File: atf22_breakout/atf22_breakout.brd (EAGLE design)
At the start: 18.8 x 36.8 mm, 4 parts

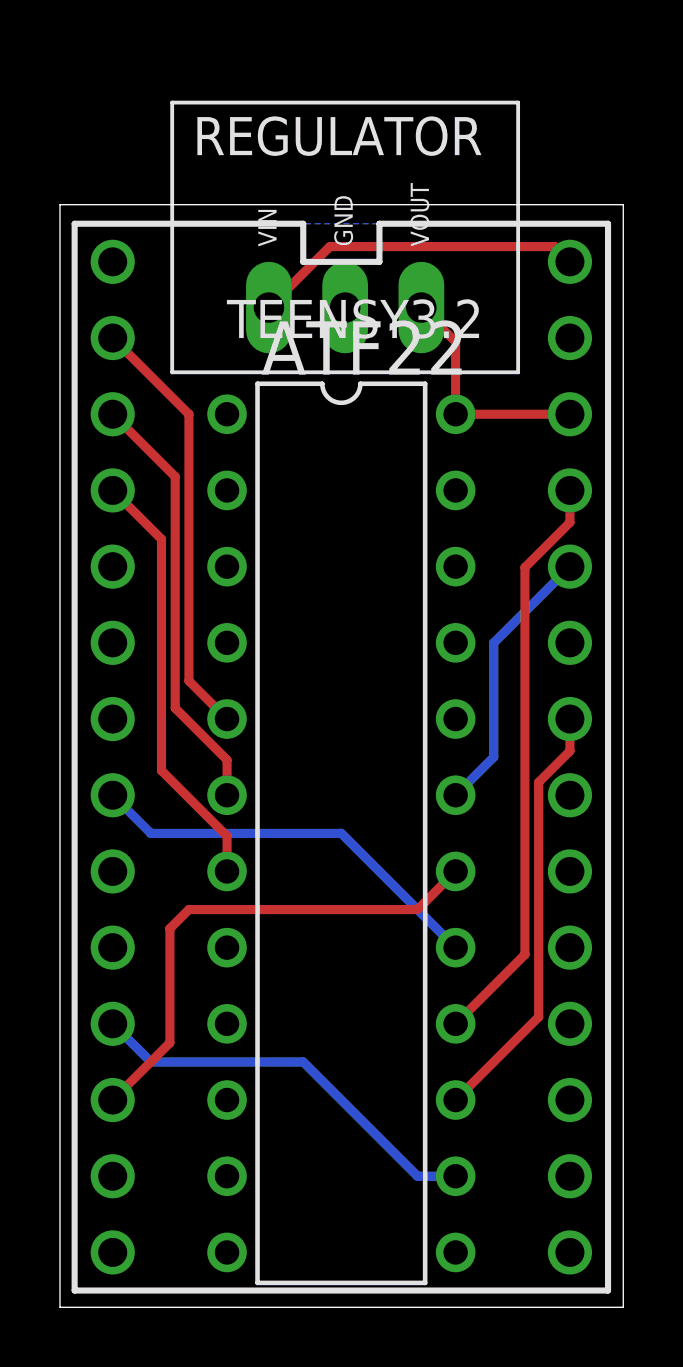
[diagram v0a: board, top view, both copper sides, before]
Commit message: Fixed ATF22 Breakout
Moved voltage regulator so it fits on the board.
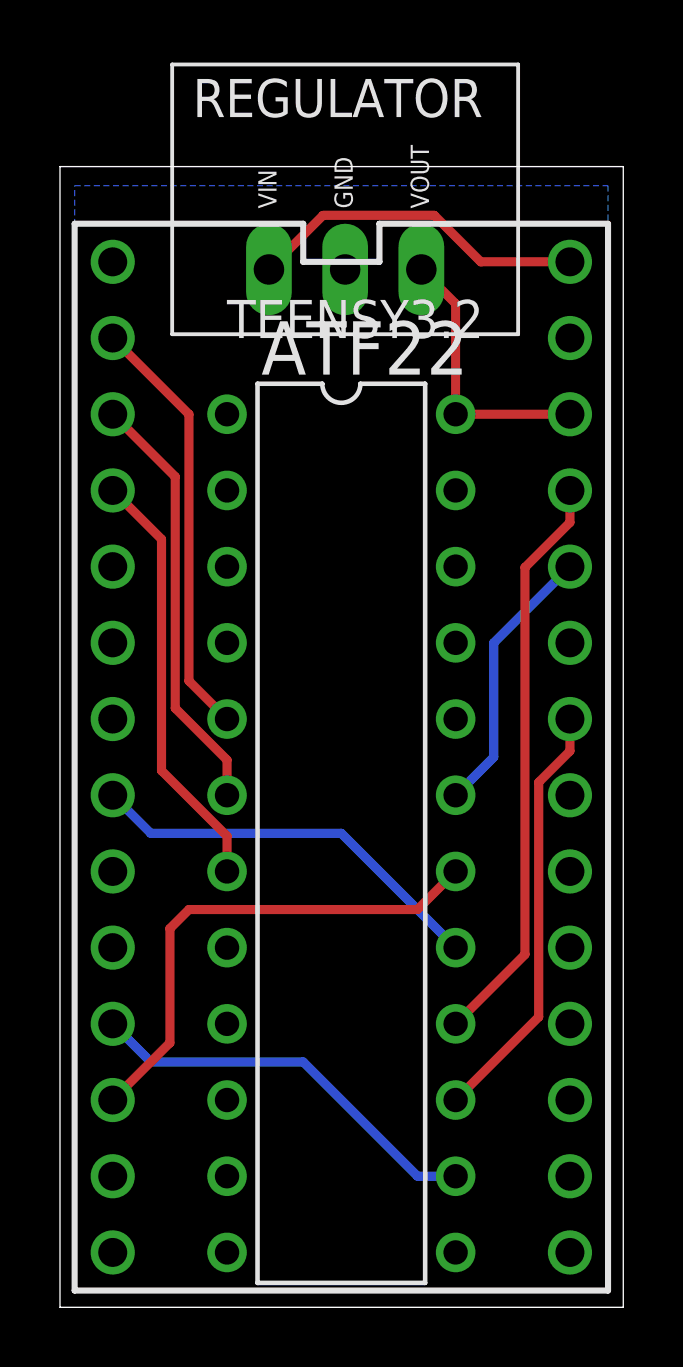
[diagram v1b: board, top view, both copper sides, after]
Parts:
- moved REGULATOR 1.27 mm to (10.3, 39.1)
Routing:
- net 3.3V: track 7.84 -> 9.11 mm
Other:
- board size 18.8 x 36.8 mm -> 18.8 x 38 mm
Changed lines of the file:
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@@
 <drawing>
 <settings>
-<setting alwaysvectorfont="yes"/>
+<setting alwaysvectorfont="no"/>
 <setting verticaltext="up"/>
 </settings>
@@
 <board>
 <plain>
-<wire x1="19.558" y1="37.465" x2="0.782" y2="37.465" width="0" layer="20"/>
-<wire x1="0.782" y1="37.465" x2="0.782" y2="0.711" width="0" layer="20"/>
+<wire x1="19.558" y1="38.735" x2="0.782" y2="38.735" width="0" layer="20"/>
+<wire x1="0.782" y1="38.735" x2="0.782" y2="0.711" width="0" layer="20"/>
 <wire x1="0.782" y1="0.711" x2="19.558" y2="0.711" width="0" layer="20"/>
-<wire x1="19.558" y1="0.711" x2="19.558" y2="37.465" width="0" layer="20"/>
+<wire x1="19.558" y1="0.711" x2="19.558" y2="38.735" width="0" layer="20"/>
 <text x="8.89" y="2.54" size="0.762" layer="22" font="vector" ratio="20" rot="MR90">ATF22 Breakout
 Designed by: Jack Proudfoot
@@
 <element name="ATF22" library="Custom_old" package="PDIP-T24" value="ATF22" x="10.16" y="16.51" rot="R270"/>
 <element name="TEENSY3.2" library="Teensy" package="TEENSY_3.0-3.2&amp;LC_DIL" value="TEENSY_3.1-3.2_DIL" x="10.16" y="19.05"/>
-<element name="REGULATOR" library="2018" package="V78W" value="" x="10.287" y="37.846"/>
+<element name="REGULATOR" library="2018" package="V78W" value="" x="10.287" y="39.116"/>
 <element name="U$1" library="Custom_old" package="DEV" value="" x="7.62" y="19.05" rot="MR90"/>
 </elements>
@@
 <contactref element="ATF22" pad="24"/>
 <contactref element="TEENSY3.2" pad="3.3V"/>
-<wire x1="12.827" y1="34.036" x2="13.97" y2="32.893" width="0.3048" layer="1"/>
-<wire x1="13.97" y1="32.893" x2="13.97" y2="30.48" width="0.3048" layer="1"/>
 <wire x1="13.97" y1="30.48" x2="17.78" y2="30.48" width="0.3048" layer="1"/>
+<wire x1="13.97" y1="30.48" x2="13.97" y2="34.163" width="0.3048" layer="1"/>
+<wire x1="13.97" y1="34.163" x2="12.827" y2="35.306" width="0.3048" layer="1"/>
 </signal>
 <signal name="VIN">
 <contactref element="TEENSY3.2" pad="VIN"/>
 <contactref element="REGULATOR" pad="IN"/>
-<wire x1="7.747" y1="34.036" x2="9.779" y2="36.068" width="0.3048" layer="1"/>
-<wire x1="17.272" y1="36.068" x2="17.78" y2="35.56" width="0.3048" layer="1"/>
-<wire x1="9.779" y1="36.068" x2="17.272" y2="36.068" width="0.3048" layer="1"/>
+<wire x1="14.8077625" y1="35.56" x2="17.78" y2="35.56" width="0.3048" layer="1"/>
+<wire x1="13.2583625" y1="37.1094" x2="14.8077625" y2="35.56" width="0.3048" layer="1"/>
+<wire x1="9.5504" y1="37.1094" x2="13.2583625" y2="37.1094" width="0.3048" layer="1"/>
+<wire x1="7.747" y1="35.306" x2="9.5504" y2="37.1094" width="0.3048" layer="1"/>
 </signal>
 <signal name="GND">
@@
 <contactref element="TEENSY3.2" pad="GND"/>
 <polygon width="0.3048" layer="16">
-<vertex x="19.05" y="36.83"/>
+<vertex x="19.05" y="38.1"/>
 <vertex x="19.05" y="1.27"/>
 <vertex x="1.27" y="1.27"/>
-<vertex x="1.27" y="36.83"/>
+<vertex x="1.27" y="38.1"/>
 </polygon>
 <contactref element="REGULATOR" pad="GND"/>
